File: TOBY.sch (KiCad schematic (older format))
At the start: 30 parts

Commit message: added footprintadded footprintss
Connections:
- net +1V8: now reaches U?.5 (V_INT)
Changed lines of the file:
@@
 $Descr A4 11693 8268
 encoding utf-8
-Sheet 3 7
+Sheet 3 8
 Title ""
 Date "2016-04-12"
@@
 Connection ~ 1150 1650
 Connection ~ 4000 1750
+$Comp
+L +1V8 #PWR?
+U 1 1 57168AFB
+P 7400 1500
+F 0 "#PWR?" H 7400 1350 50  0001 C CNN
+F 1 "+1V8" H 7400 1640 50  0000 C CNN
+F 2 "" H 7400 1500 50  0000 C CNN
+F 3 "" H 7400 1500 50  0000 C CNN
+	1    7400 1500
+	1    0    0    -1
+$EndComp
+Wire Wire Line
+	7150 1600 7400 1600
+Wire Wire Line
+	7400 1600 7400 1500
 $EndSCHEMATC

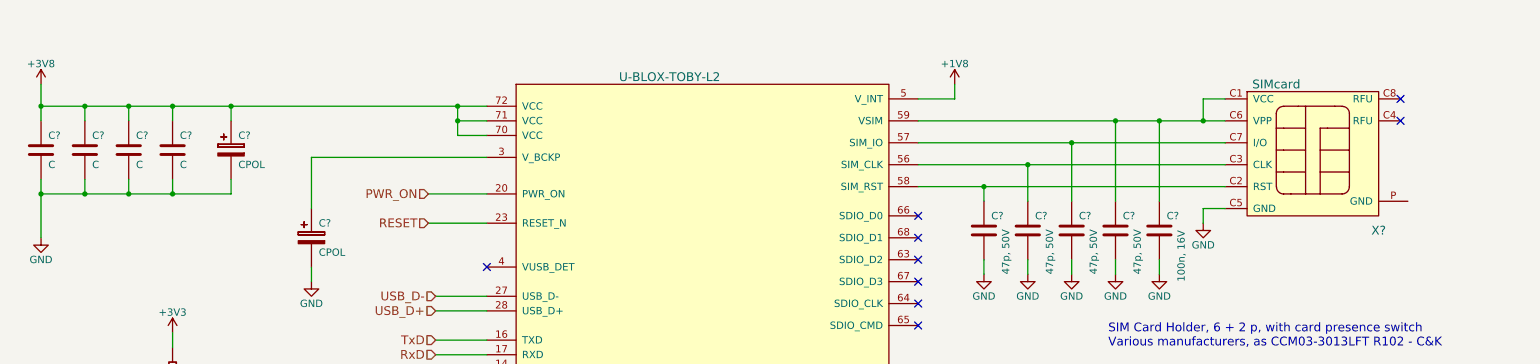
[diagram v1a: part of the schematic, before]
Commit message: SimCard footprint ergänzt
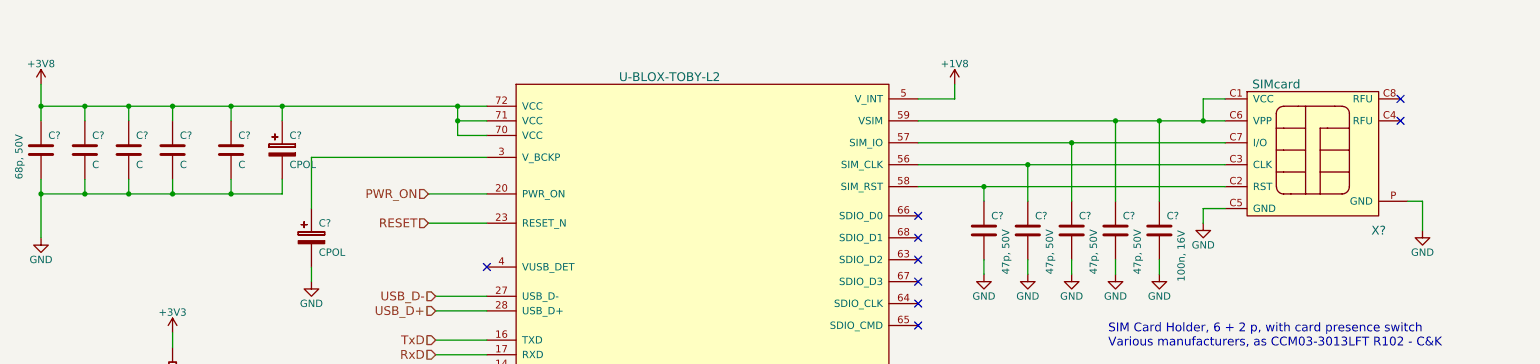
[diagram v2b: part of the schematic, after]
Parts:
- added C?: C, symbol C
- C?: value C -> 68p, 50V; footprint (none) -> Passives:C0402N
- X?: footprint (none) -> Connector:NANO_SIM_693043020611
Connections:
- net +3V8: now also C?.1
- net GND: now also X?.P (GND), C?.2
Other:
- moved on the sheet: C?
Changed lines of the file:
@@
 F 0 "X?" H 10300 1400 60  0000 C CNN
 F 1 "SIMcard" H 9600 2400 60  0000 C CNN
-F 2 "" H 9850 1950 60  0000 C CNN
+F 2 "Connector:NANO_SIM_693043020611" H 9850 1950 60  0001 C CNN
 F 3 "" H 9850 1950 60  0000 C CNN
 	1    9850 1950
@@
 P 1150 1950
 F 0 "C?" H 1200 2050 50  0000 L CNN
-F 1 "C" H 1200 1850 50  0000 L CNN
-F 2 "" H 1188 1800 30  0000 C CNN
+F 1 "68p, 50V" V 1000 1750 50  0000 L CNN
+F 2 "Passives:C0402N" H 1188 1800 30  0001 C CNN
 F 3 "" H 1200 2050 60  0000 C CNN
 	1    1150 1950
@@
 L CPOL C?
 U 1 1 570F9E95
-P 2450 1950
-F 0 "C?" H 2500 2050 50  0000 L CNN
-F 1 "CPOL" H 2500 1850 50  0000 L CNN
-F 2 "" H 2488 1800 30  0000 C CNN
-F 3 "" H 2450 1950 60  0000 C CNN
-	1    2450 1950
+P 2800 1950
+F 0 "C?" H 2850 2050 50  0000 L CNN
+F 1 "CPOL" H 2850 1850 50  0000 L CNN
+F 2 "" H 2838 1800 30  0000 C CNN
+F 3 "" H 2800 1950 60  0000 C CNN
+	1    2800 1950
 	1    0    0    -1
 $EndComp
@@
 	1150 2150 1150 2550
 Wire Wire Line
-	1150 2250 2450 2250
+	1150 2250 2800 2250
 Wire Wire Line
 	2450 2250 2450 2150
@@
 Wire Wire Line
 	7400 1600 7400 1500
+$Comp
+L GND #PWR?
+U 1 1 571D4F40
+P 10600 2500
+F 0 "#PWR?" H 10600 2250 50  0001 C CNN
+F 1 "GND" H 10600 2350 50  0000 C CNN
+F 2 "" H 10600 2500 50  0000 C CNN
+F 3 "" H 10600 2500 50  0000 C CNN
+	1    10600 2500
+	1    0    0    -1
+$EndComp
+Wire Wire Line
+	10600 2500 10600 2300
+Wire Wire Line
+	10600 2300 10500 2300
+$Comp
+L C C?
+U 1 1 571D7BE4
+P 2450 1950
+F 0 "C?" H 2500 2050 50  0000 L CNN
+F 1 "C" H 2500 1850 50  0000 L CNN
+F 2 "" H 2488 1800 30  0000 C CNN
+F 3 "" H 2500 2050 60  0000 C CNN
+	1    2450 1950
+	1    0    0    -1
+$EndComp
+Wire Wire Line
+	2800 2250 2800 2150
+Connection ~ 2450 2250
+Wire Wire Line
+	2800 1750 2800 1650
+Connection ~ 2800 1650
 $EndSCHEMATC

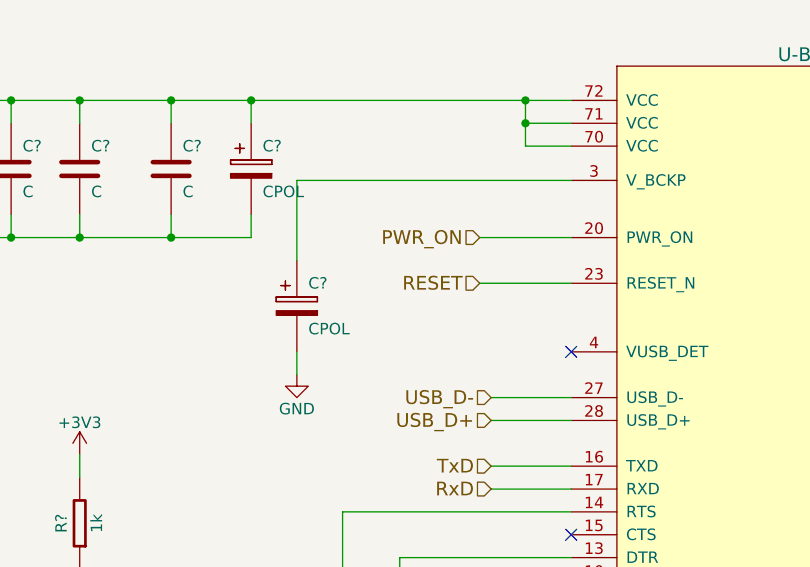
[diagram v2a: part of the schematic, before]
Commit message: LAN Transformer footprint ergänzt
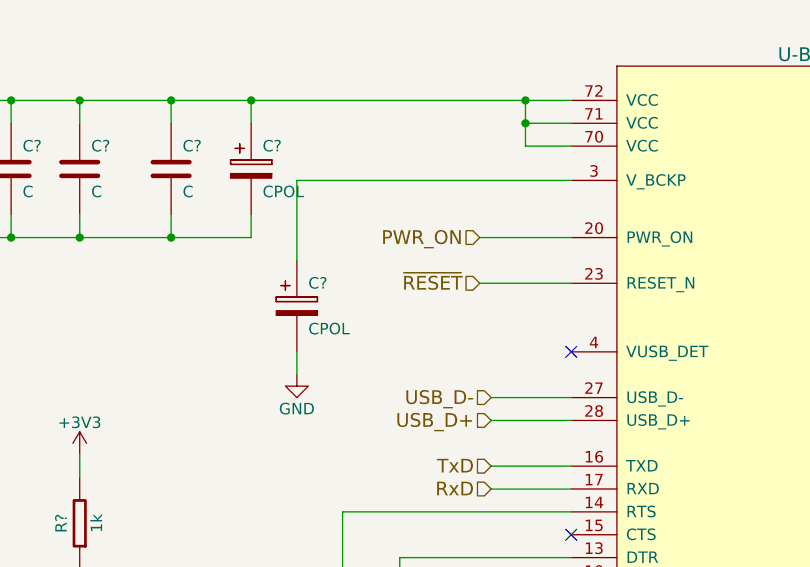
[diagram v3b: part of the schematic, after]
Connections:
- net RESET renamed ~RESET
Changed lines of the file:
@@
 PWR_ON
 Text HLabel 3800 2450 0    60   Input ~ 0
-RESET
+~RESET
 Wire Wire Line
 	3800 2250 4200 2250

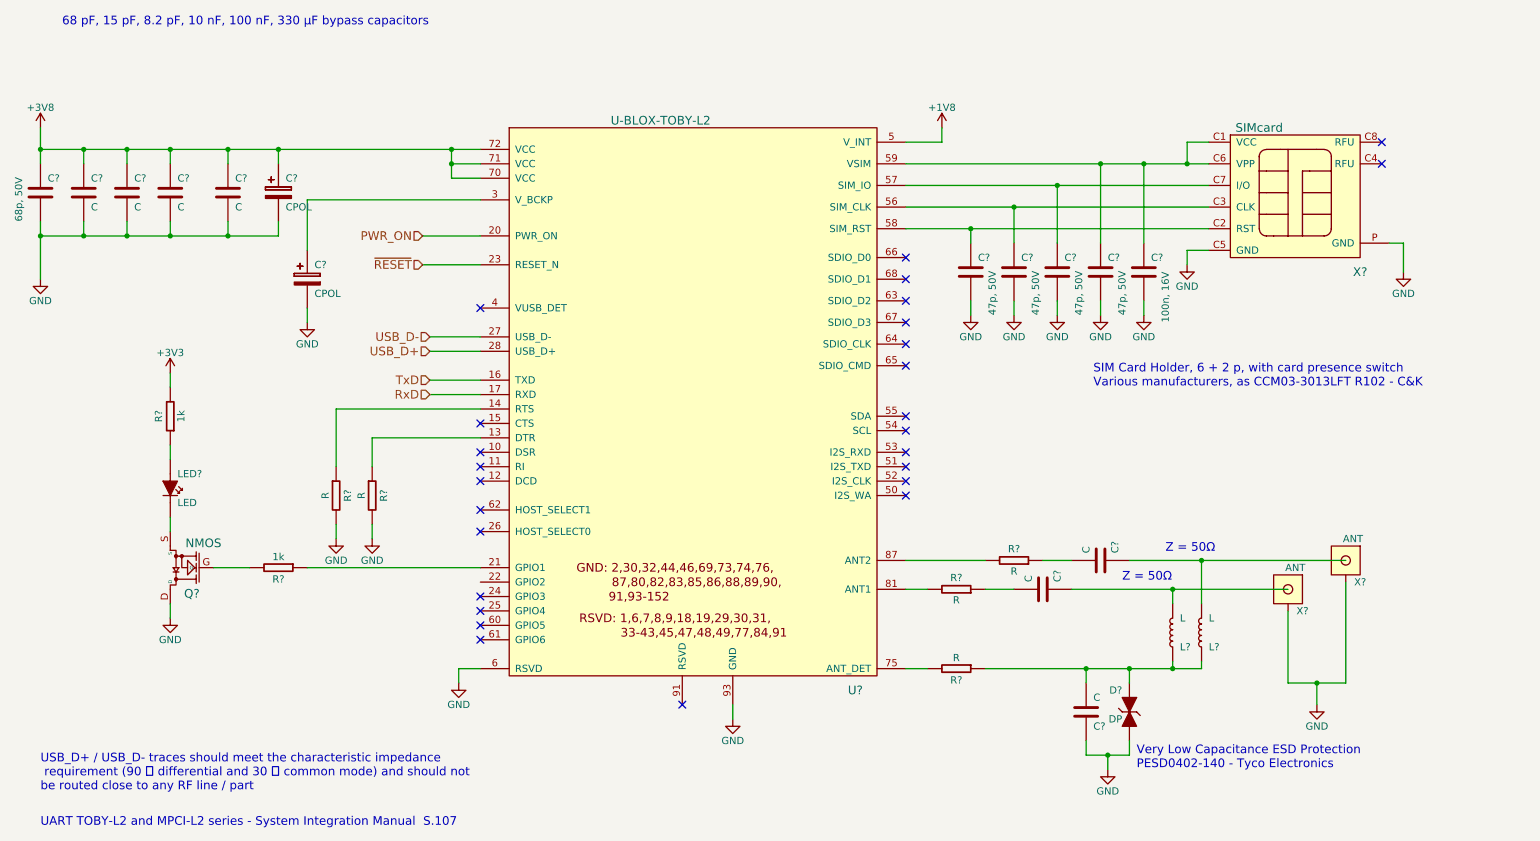
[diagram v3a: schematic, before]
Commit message: footprints ergänzt
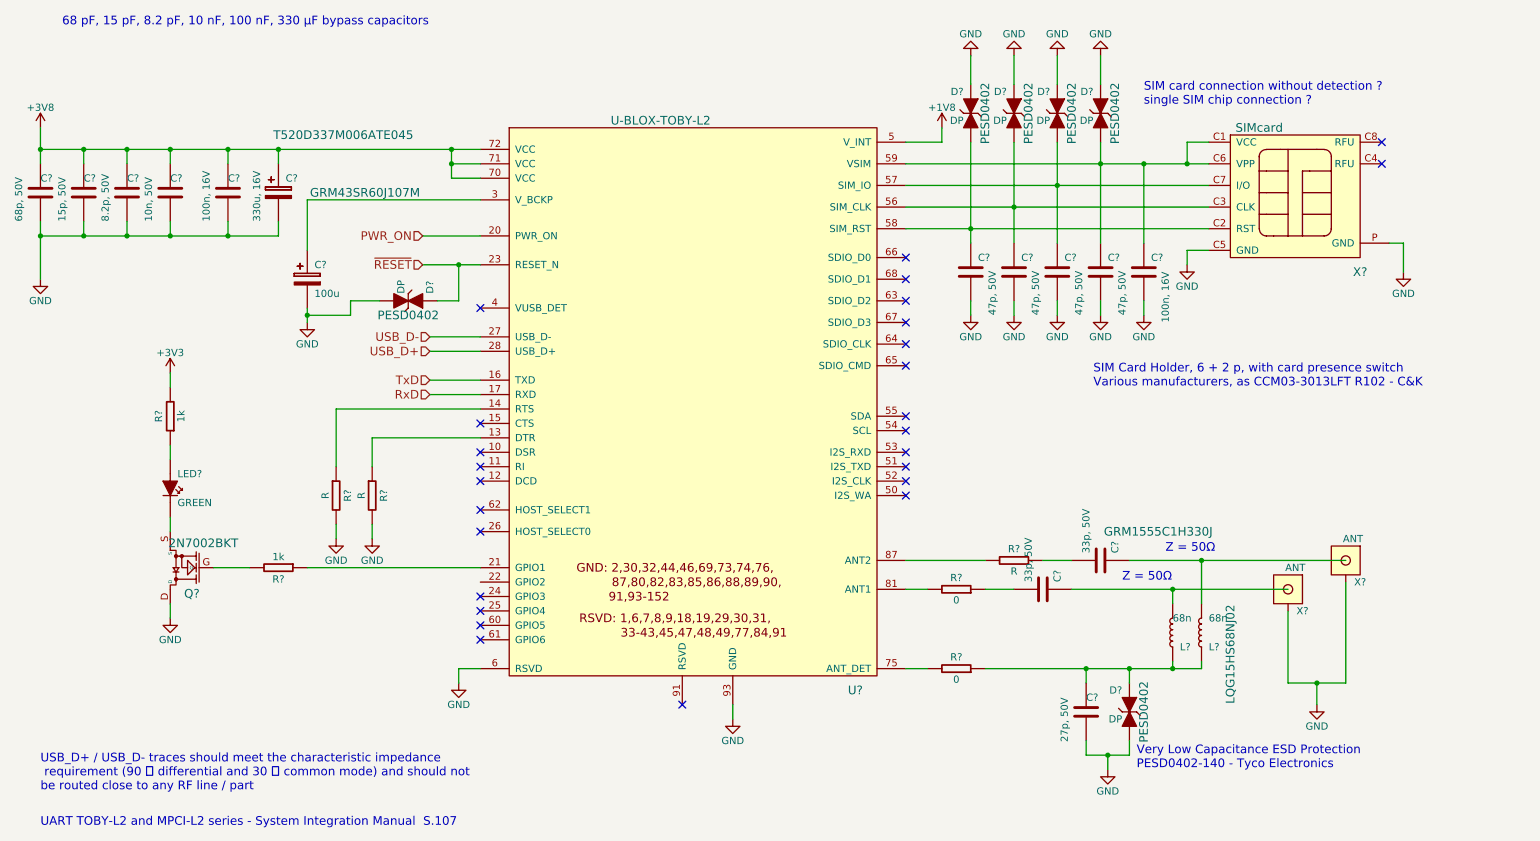
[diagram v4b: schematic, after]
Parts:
- removed C? (x4): C, symbol C
- removed R?: R, symbol R
- added C?: 8.2p, 50V, Passives:C0402N, symbol C
- added C?: 10n, 50V, Passives:C0402N, symbol C
- added C?: 100n, 16V, Passives:C0402N, symbol C
- added C?: 33p, 50V, Passives:C0402N, symbol C
- added D? (x5): DP, Passives:D_0402, symbol DP
- added R?: 0, Passives:R0402N, symbol R
- C?: value C -> 33p, 50V; footprint (none) -> Passives:C0402N
- C?: value C -> 27p, 50V; footprint (none) -> Passives:C0402N
- C?: value C -> 15p, 50V; footprint (none) -> Passives:C0402N
- C?: value CPOL -> 330u, 16V
- C?: value CPOL -> 100u
- D?: footprint (none) -> Passives:D_0402
- L? (x2): value L -> 68n; footprint (none) -> Passives:L0402N
- LED?: value LED -> GREEN; footprint (none) -> Passives:LED0603N
- Q?: value NMOS -> 2N7002BKT; footprint (none) -> Transistor:SOT416_GSD
- R?: value R -> 0; footprint (none) -> Passives:R0402N
- X? (x2): footprint (none) -> Connector:U.FL-R-SMT
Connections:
- net +3V8: now also C?.1, C?.1, C?.1
- net GND: now also C?.2, C?.2, C?.2, D?.A, D?.A, D?.A, D?.A, D?.C
- net ~RESET: now also D?.A
- net at C?.1, U?.56 (SIM_CLK), X?.C3 (CLK): now also D?.C
- net at C?.1, U?.57 (SIM_IO), X?.C7 (I/O): now also D?.C
- net at C?.1, U?.58 (SIM_RST), X?.C2 (RST): now also D?.C
- net at C?.1, C?.1, U?.59 (VSIM)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: now also D?.C
- net at U?.75 (ANT_DET): now also R?.2
- net at R?.1: now also C?.2
- net at L?.2, X?.1 (SIG): now also C?.1
- net at C?.2, D?.A, L?.1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: now also R?.1
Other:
- note added: "SIM card connection without detection ?\nsingle SIM chip connection ?"

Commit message: added some footprints
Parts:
- removed R?: R, symbol R
- added R307: 0, Passives:R0402N, symbol R
- U301: renamed from U?; footprint (none) -> Communication:UBLOX_TOBY_L210
- gave numbers to parts that had none: 34
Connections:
- net at U301.87 (ANT2): now also R307.2
- net at C314.2: now also R307.1

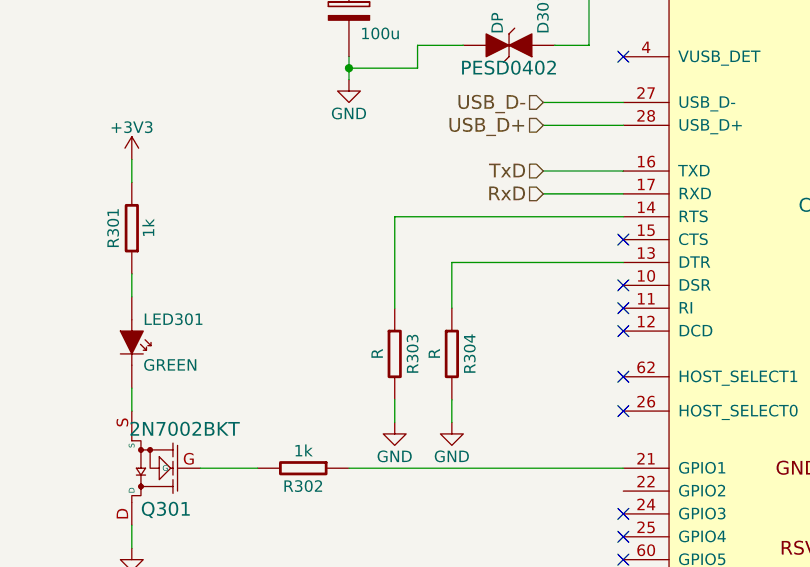
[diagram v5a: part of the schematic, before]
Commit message: added footprints
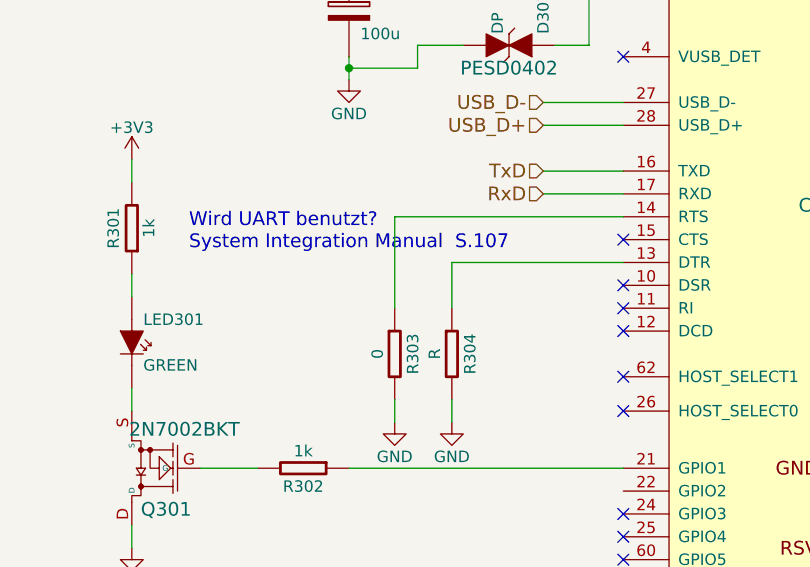
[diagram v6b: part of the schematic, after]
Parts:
- C306: footprint (none) -> Passives:T520D
- R303: value R -> 0; footprint (none) -> Passives:R0402N
- R304: footprint (none) -> Passives:R0402N
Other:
- note added: "Wird UART benutzt?\nSystem Integration Manual S.107"
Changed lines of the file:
@@
 F 0 "C306" H 2850 2050 50  0000 L CNN
 F 1 "330u, 16V" V 2650 1750 50  0000 L CNN
-F 2 "" H 2838 1800 30  0001 C CNN
+F 2 "Passives:T520D" H 2838 1800 30  0001 C CNN
 F 3 "T520D337M006ATE045" H 3250 2350 60  0000 C CNN
 	1    2800 1950
@@
 P 3200 4050
 F 0 "R303" V 3280 4050 50  0000 C CNN
-F 1 "R" V 3125 4050 50  0000 C CNN
-F 2 "" V 3130 4050 30  0001 C CNN
+F 1 "0" V 3125 4050 50  0000 C CNN
+F 2 "Passives:R0402N" V 3130 4050 30  0001 C CNN
 F 3 "" H 3200 4050 30  0000 C CNN
 	1    3200 4050
@@
 F 0 "R304" V 3530 4050 50  0000 C CNN
 F 1 "R" V 3375 4050 50  0000 C CNN
-F 2 "" V 3380 4050 30  0001 C CNN
+F 2 "Passives:R0402N" V 3380 4050 30  0001 C CNN
 F 3 "" H 3450 4050 30  0000 C CNN
 	1    3450 4050
@@
 	0    1    -1   0
 $EndComp
+Text Notes 2300 3600 0    60   ~ 0
+Wird UART benutzt?\nSystem Integration Manual  S.107
 $EndSCHEMATC
